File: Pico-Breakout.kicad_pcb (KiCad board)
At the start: 2 copper layers, 38.1 x 52.1 mm, 3 parts, among them J101 Conn_01x20, J102 Conn_01x20, U101 Pico

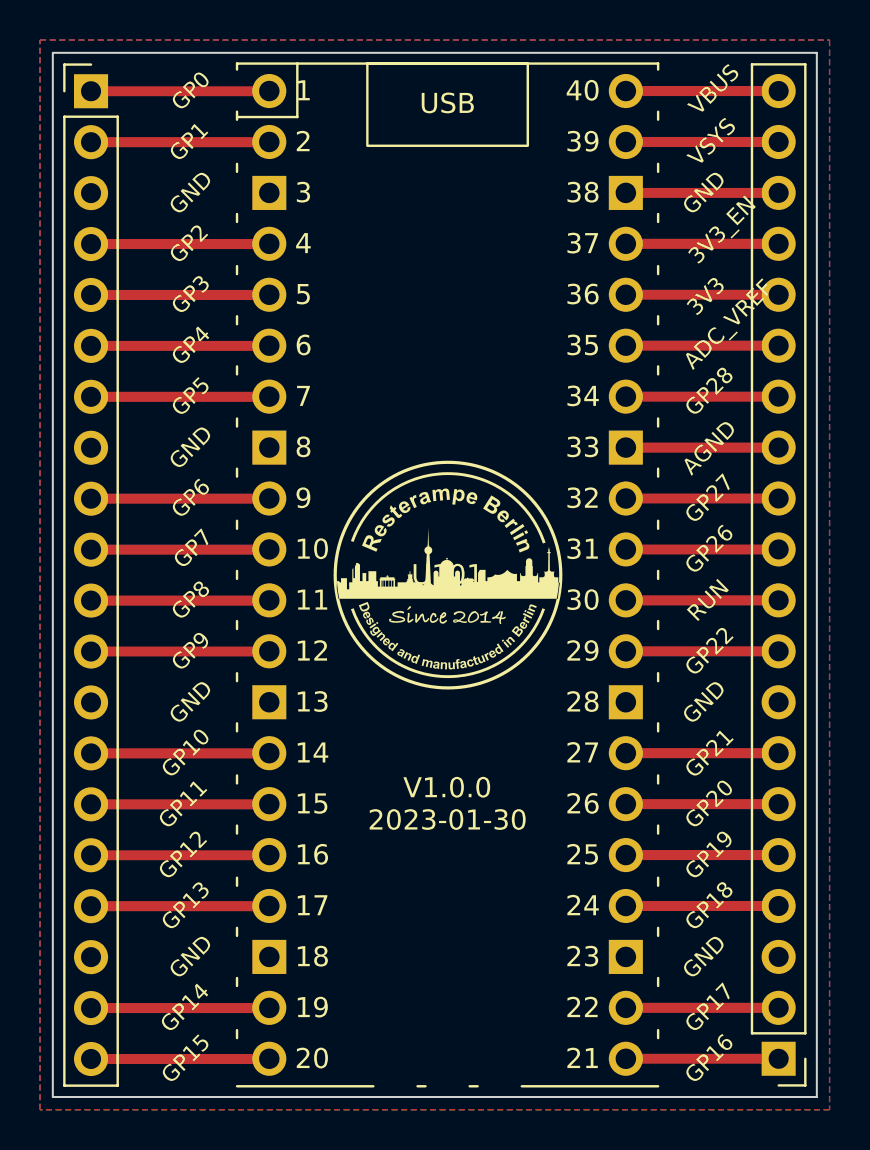
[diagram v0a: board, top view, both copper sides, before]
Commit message: Documentation update, name of board on PCB
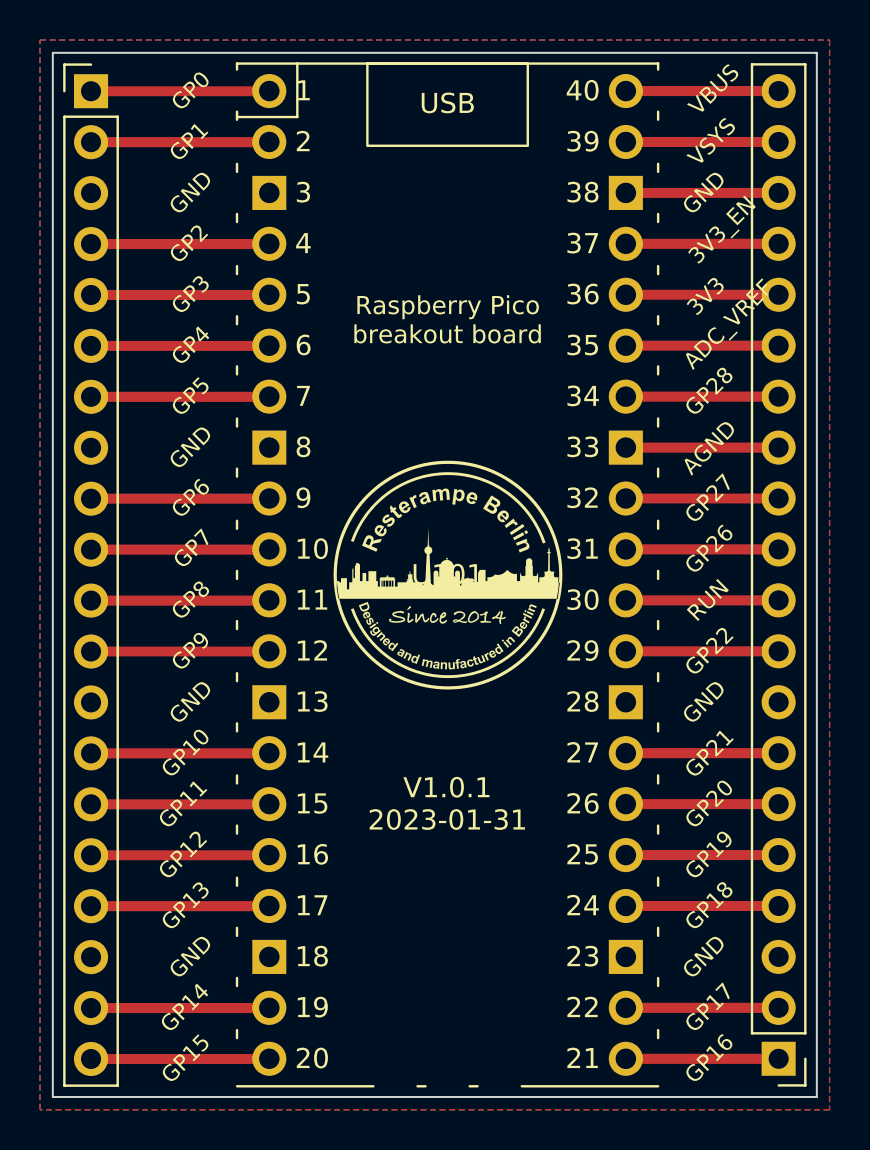
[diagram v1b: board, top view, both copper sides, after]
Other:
- board text added: "Raspberry Pico breakout board"
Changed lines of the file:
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@@
   (title_block
     (title "Raspberry Pico breakout board")
-    (date "2023-01-30")
-    (rev "1.0.0")
+    (date "2023-01-31")
+    (rev "1.0.1")
     (company "Resterampe Berlin ")
     (comment 3 "https://creativecommons.org/licenses/by-nc/4.0 ")
@@
     (effects (font (size 1 1) (thickness 0.15)) (justify left))
   )
+  (gr_text "Raspberry Pico\nbreakout board" (at 157.48 82.55) (layer "F.SilkS")
+    (effects (font (size 0.9 0.9) (thickness 0.15)))
+  )
   (gr_text "12" (at 149.86 99.06) (layer "F.SilkS")
